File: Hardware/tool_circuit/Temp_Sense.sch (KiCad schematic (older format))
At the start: 1 part, among them J2 Conn_01x03_Female

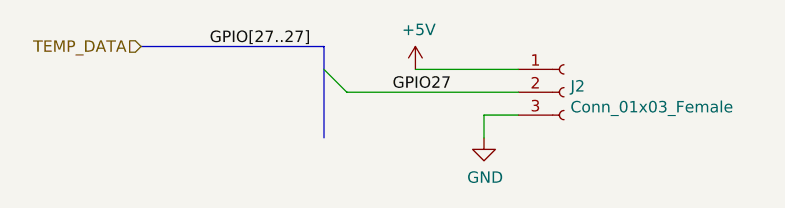
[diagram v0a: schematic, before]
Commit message: schematic LEDs + switch
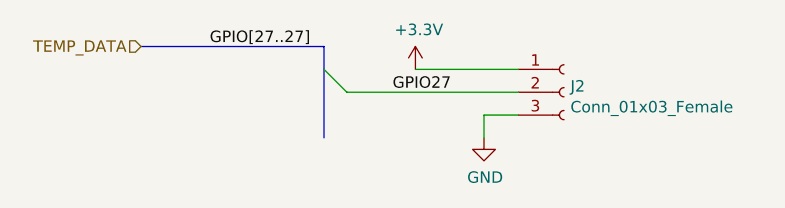
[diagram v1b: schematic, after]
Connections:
- net +5V renamed +3V3
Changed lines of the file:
@@
 Wire Wire Line
 	5350 3600 5350 3700
-$Comp
-L power:+5V #PWR08
-U 1 1 614AFBC4
-P 5050 3400
-F 0 "#PWR08" H 5050 3250 50  0001 C CNN
-F 1 "+5V" H 5065 3573 50  0000 C CNN
-F 2 "" H 5050 3400 50  0001 C CNN
-F 3 "" H 5050 3400 50  0001 C CNN
-	1    5050 3400
-	1    0    0    -1
-$EndComp
 Wire Wire Line
 	5050 3400 5500 3400
@@
 Text Label 4150 3300 0    50   ~ 0
 GPIO[27..27]
+$Comp
+L power:+3.3V #PWR0102
+U 1 1 6153FBB6
+P 5050 3400
+F 0 "#PWR0102" H 5050 3250 50  0001 C CNN
+F 1 "+3.3V" H 5065 3573 50  0000 C CNN
+F 2 "" H 5050 3400 50  0001 C CNN
+F 3 "" H 5050 3400 50  0001 C CNN
+	1    5050 3400
+	1    0    0    -1
+$EndComp
 Wire Bus Line
 	4650 3300 4650 3700

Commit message: made some post review changes
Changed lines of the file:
@@
 Wire Wire Line
 	5050 3400 5500 3400
-Text HLabel 3850 3300 0    50   Input ~ 0
+Text HLabel 3850 3300 0    50   BiDi ~ 0
 TEMP_DATA
 Wire Bus Line
@@
 Text Label 4950 3500 0    50   ~ 0
 GPIO27
-Text Label 4150 3300 0    50   ~ 0
-GPIO[27..27]
 $Comp
 L power:+3.3V #PWR0102

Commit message: pcb revisions
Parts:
- J2: value Conn_01x03_Female -> Temp_Sense
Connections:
- net GPIO27 renamed GPIO27_GEN2
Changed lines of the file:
@@
 P 5700 3500
 F 0 "J2" H 5728 3526 50  0000 L CNN
-F 1 "Conn_01x03_Female" H 5728 3435 50  0000 L CNN
+F 1 "Temp_Sense" H 5728 3435 50  0000 L CNN
 F 2 "Connector_PinHeader_2.54mm:PinHeader_1x03_P2.54mm_Vertical" H 5700 3500 50  0001 C CNN
 F 3 "~" H 5700 3500 50  0001 C CNN
@@
 Wire Wire Line
 	5050 3400 5500 3400
-Text HLabel 3850 3300 0    50   BiDi ~ 0
-TEMP_DATA
-Wire Bus Line
-	3850 3300 4650 3300
-Entry Wire Line
-	4650 3400 4750 3500
-Wire Wire Line
-	4750 3500 5500 3500
-Text Label 4950 3500 0    50   ~ 0
-GPIO27
 $Comp
 L power:+3.3V #PWR08
@@
 	1    0    0    -1
 $EndComp
-Wire Bus Line
-	4650 3300 4650 3700
+Text GLabel 5250 3500 0    50   BiDi ~ 0
+GPIO27_GEN2
+Wire Wire Line
+	5500 3500 5250 3500
 $EndSCHEMATC
